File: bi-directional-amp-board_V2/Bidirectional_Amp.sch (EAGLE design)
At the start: 105 parts, among them J1 142-0701-851_ALT, J2 142-0701-851_ALT, J3 142-0701-851_ALT, J4 142-0701-851_ALT, J6 142-0701-851_ALT, J7 142-0701-851_ALT, SW1 TL36PO, U1 SN74LVC1G32DBVR, U10 TQP9111, U11 SN74LV1T34DBVR, U12 SN74LVC1G32DBVR, U2 LTC6994-1, U3 LTC6994-1, U4 TQP3M903X, U5 TQP3M903X, U6 SN74LV1T34DBVR, U7 QPC1022, U8 QPC1022, U9 SN74LV1T34DBVR

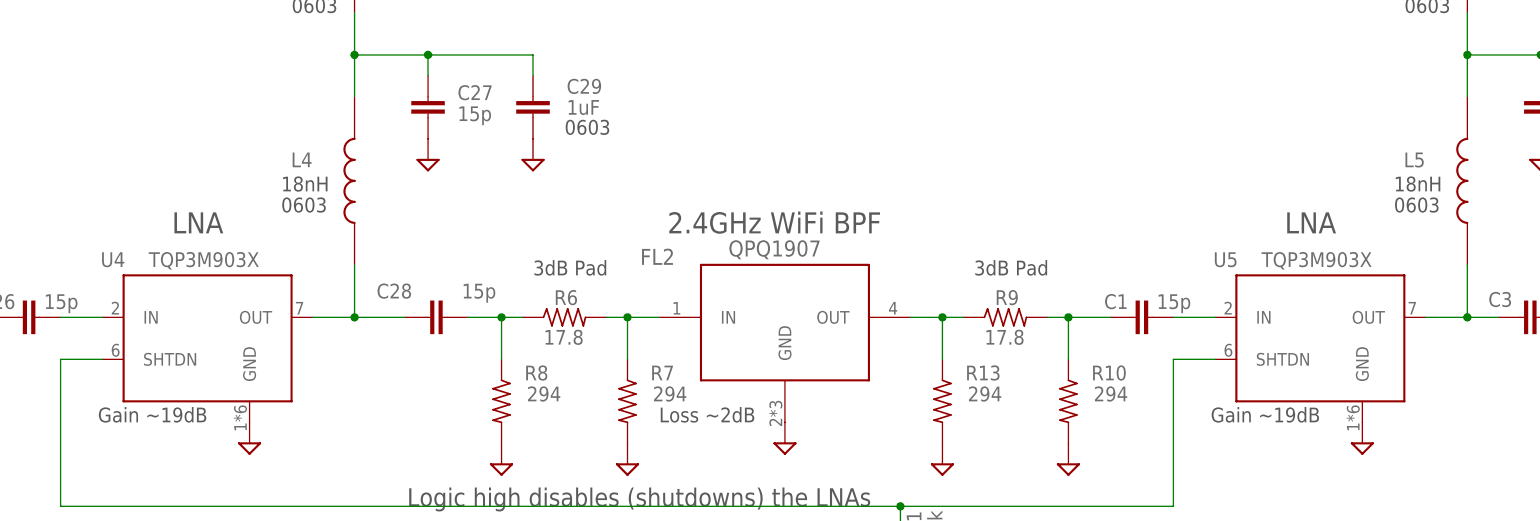
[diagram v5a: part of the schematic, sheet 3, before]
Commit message: Made the LNAs the correct part number.
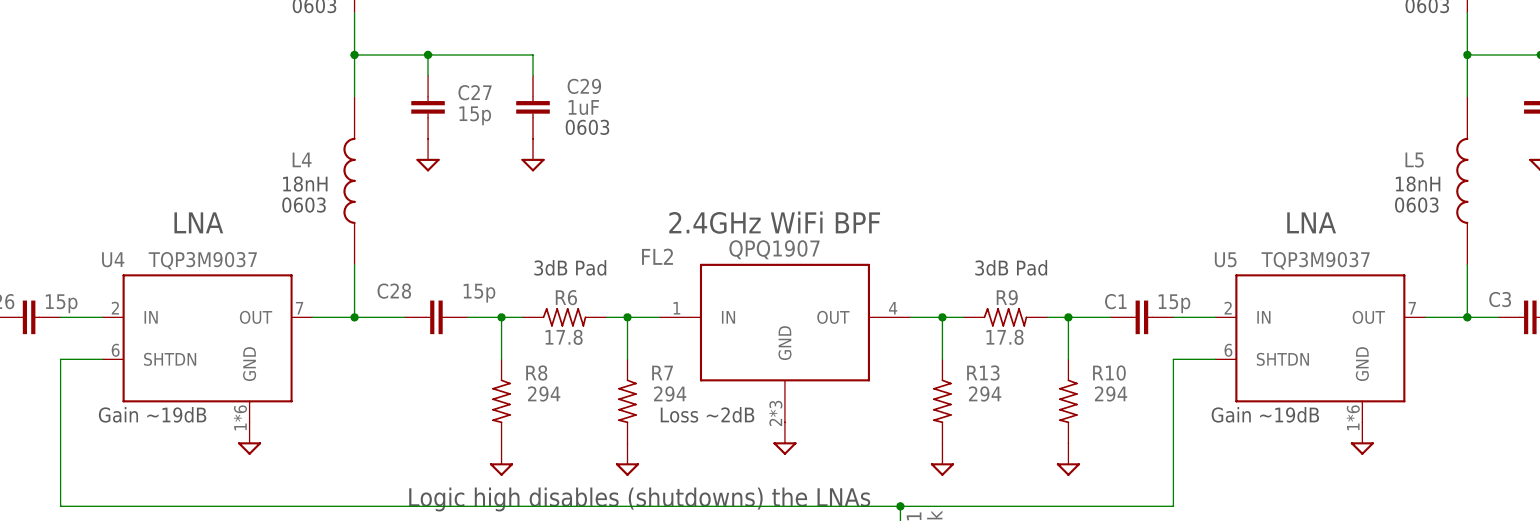
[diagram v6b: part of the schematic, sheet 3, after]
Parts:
- U4, U5: value TQP3M903X -> TQP3M9037
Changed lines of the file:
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@@
 <attribute name="MPN" value="ERJ-2GEJ103X"/>
 </part>
-<part name="U4" library="U-Qorvo-TQP3M903x-LNA" deviceset="TQP3M903X" device="">
+<part name="U4" library="U-Qorvo-TQP3M903x-LNA" deviceset="TQP3M903X" device="" value="TQP3M9037">
 <attribute name="MFR" value="Qorvo"/>
 <attribute name="MPN" value="TQP3M9037 "/>
@@
 <attribute name="MPN" value="0603CS-18NXJLW"/>
 </part>
-<part name="U5" library="U-Qorvo-TQP3M903x-LNA" deviceset="TQP3M903X" device="">
+<part name="U5" library="U-Qorvo-TQP3M903x-LNA" deviceset="TQP3M903X" device="" value="TQP3M9037">
 <attribute name="MFR" value="Qorvo"/>
 <attribute name="MPN" value="TQP3M9037 "/>
